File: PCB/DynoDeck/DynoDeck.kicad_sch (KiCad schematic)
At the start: 8 parts, among them J1 USB_C_Receptacle_USB2.0_16P, J2 E-paper, J3 CardKB, U1 E73-2G4M08S1C, U2 SX1262IMLTRT, U3 BQ25895RTW, U4 AMS1117-3.3, U5 TPS613222ADBV

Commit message: Schematic Power Circuit
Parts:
- removed U5: TPS613222ADBV, Package_TO_SOT_SMD:SOT-23-5, symbol Regulator_Switching:TPS613222ADBV
- added BT1: Batt, symbol Device:Battery
- added C1: 100n, symbol Device:C_Small
- added C10, C11, C6, C7, C8: 10u, symbol Device:C_Small
- added C12, C4: 4u7, symbol Device:C_Small
- added C2: 1u, symbol Device:C_Small
- added C3: 220n, symbol Device:C_Small
- added C5: 47n, symbol Device:C_Small
- added C9: 47u, symbol Device:C_Small
- added D1: STAT, symbol Device:LED_Small
- added D2: D_Schottky, symbol Device:D_Schottky_Small
- added L1: 2u2, symbol Device:L
- added R1, R2: 5k1, symbol Device:R_Small
- added R10, R6, R7, R9: 10k, symbol Device:R_Small
- added R11: 2k2, symbol Device:R_Small
- added R3, R4, R5: 4k7, symbol Device:R_Small
- added R8: 260, symbol Device:R_Small
- added SW1: QON, symbol Switch:SW_Push
- added U6: USBLC6-2SC6, Package_TO_SOT_SMD:SOT-23-6, symbol Power_Protection:USBLC6-2SC6
- J1: footprint (none) -> Connector_USB:USB_C_Receptacle_G-Switch_GT-USB-7010ASV
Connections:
- net +5V is gone; now on net +3V3: J3.3 (Pin_3)
- net +3V3: now also U4.2 (VO), C11.1, R3.1, R4.1, R5.1
- net GND: now also J1.A1 (GND), J1.A12 (GND), J1.B1 (GND), J1.B12 (GND), J1.SH (SHIELD), U3.17 (PGND), U3.18 (PGND), U3.25 (PGND), U4.1 (GND), BT1.2 (-), C1.2, C10.2, C11.2, C12.2, C2.2, C3.2, C4.2, C6.2, C7.2, C8.2, C9.2, R1.2, R10.2, R2.2, R6.2, R7.2, R8.2, SW1.2, U6.2 (GND)
- net SCL: now also U3.5 (SCL), R3.2; no longer J2.5 (Pin_5)
- net SDA: now also U3.6 (SDA), R4.2; no longer J2.6 (Pin_6)
- net VBUS: now reaches J1.A4 (VBUS), J1.A9 (VBUS), J1.B4 (VBUS), J1.B9 (VBUS)
- net VBUS: now also U1.27 (VBUS), U3.1 (VBUS), C1.1, C12.1, C2.1, C3.1, C9.1, D2.1 (K), U6.5 (VBUS)
- net at J1.A5 (CC1): now also R1.1
- net DIn+: now reaches J1.A6 (D+)
- net DIn+: now also J1.B6 (D+), U6.3 (I/O2)
- net DIn-: now reaches J1.A7 (D-)
- net DIn-: now also J1.B7 (D-), U6.1 (I/O1)
- net at J1.B5 (CC2): now also R2.1
- net D-: now reaches U1.29 (DM)
- net D-: now also U3.3 (D-), U6.6 (I/O1)
- net D+: now reaches U1.31 (DP)
- net D+: now also U3.2 (D+), U6.4 (I/O2)
- net SYS: now reaches U4.3 (VI)
- net SYS: now also U3.15 (SYS), U3.16 (SYS), C10.1, C7.1, C8.1, D1.2 (A), L1.2
- net at U3.10 (ILIM): now also R8.1
- net at U3.11 (TS): now also R10.1, R9.2
- net at U3.12 (~{QON}): now also SW1.1
- net BATT+: now reaches U3.13 (BAT), U3.14 (BAT)
- net BATT+: now also BT1.1 (+), C6.1
- net at U3.19 (SW), U3.20 (SW): now also C5.1, L1.1
- net at U3.21 (BTST): now also C5.2
- net at U3.22 (REGN): now also C4.1, R9.1
- net at U3.23 (PMID): now also D2.2 (A)
- net at U3.4 (STAT): now also R11.2
- net ~{INT}: now reaches U3.7 (~{INT})
- net ~{INT}: now also R5.2
- net OTG: now reaches U3.8 (OTG)
- net OTG: now also R6.1
- net ~{CE}: now reaches U3.9 (~{CE})
- net ~{CE}: now also R7.1
- new net: D1.1 (K), R11.1
- new net CLK: J2.5 (Pin_5)
- new net MOSI: J2.6 (Pin_6)
- no-connect marks 0 -> 3
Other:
- note added: "USBC + ESD"
- moved on the sheet: J1, J2, J3, U1A, U1C, U2, U3, U4

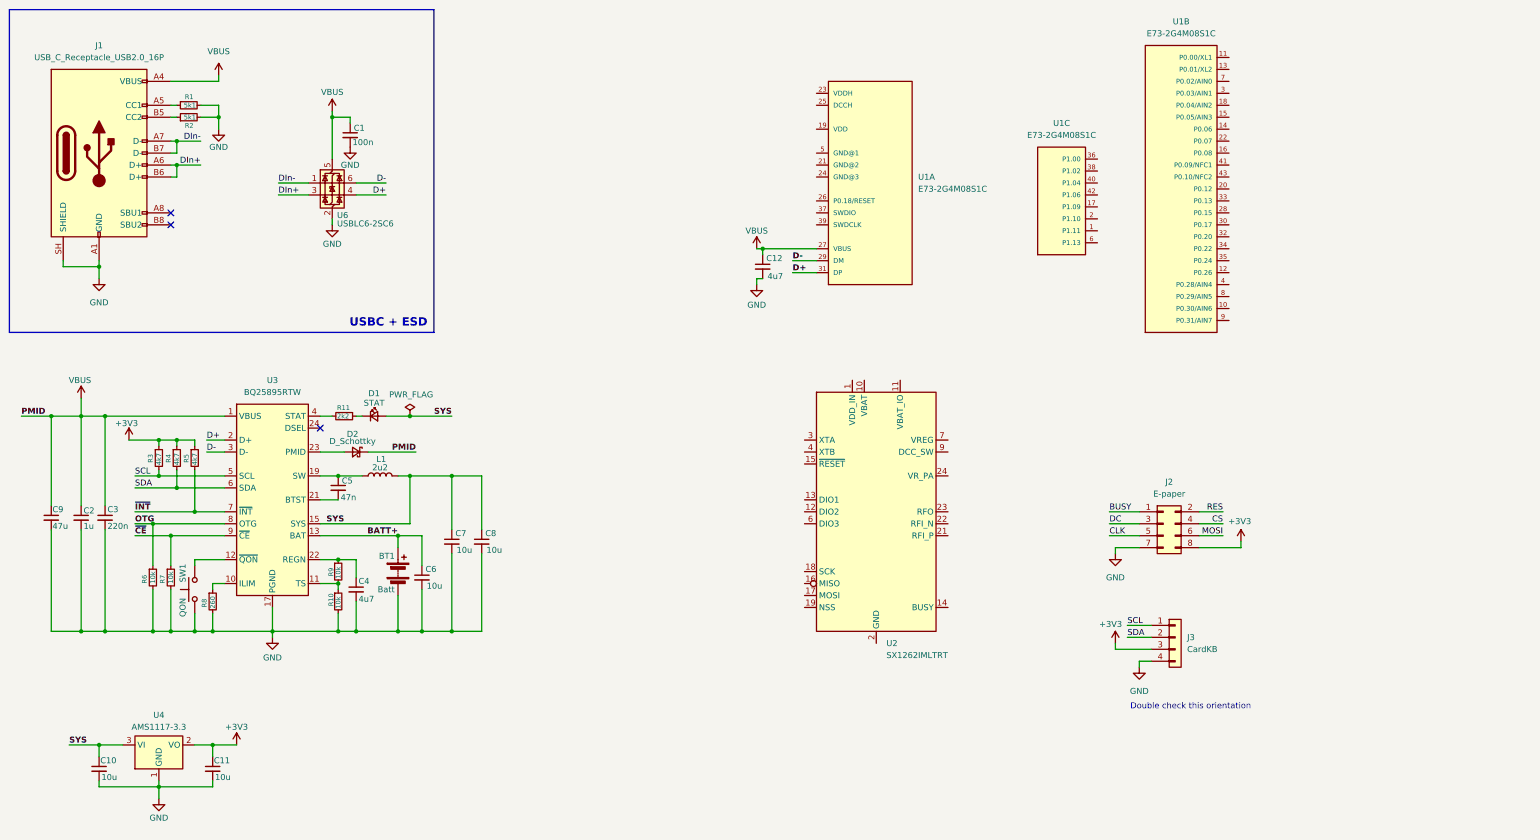
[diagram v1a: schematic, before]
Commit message: Power for nRf + SX1262
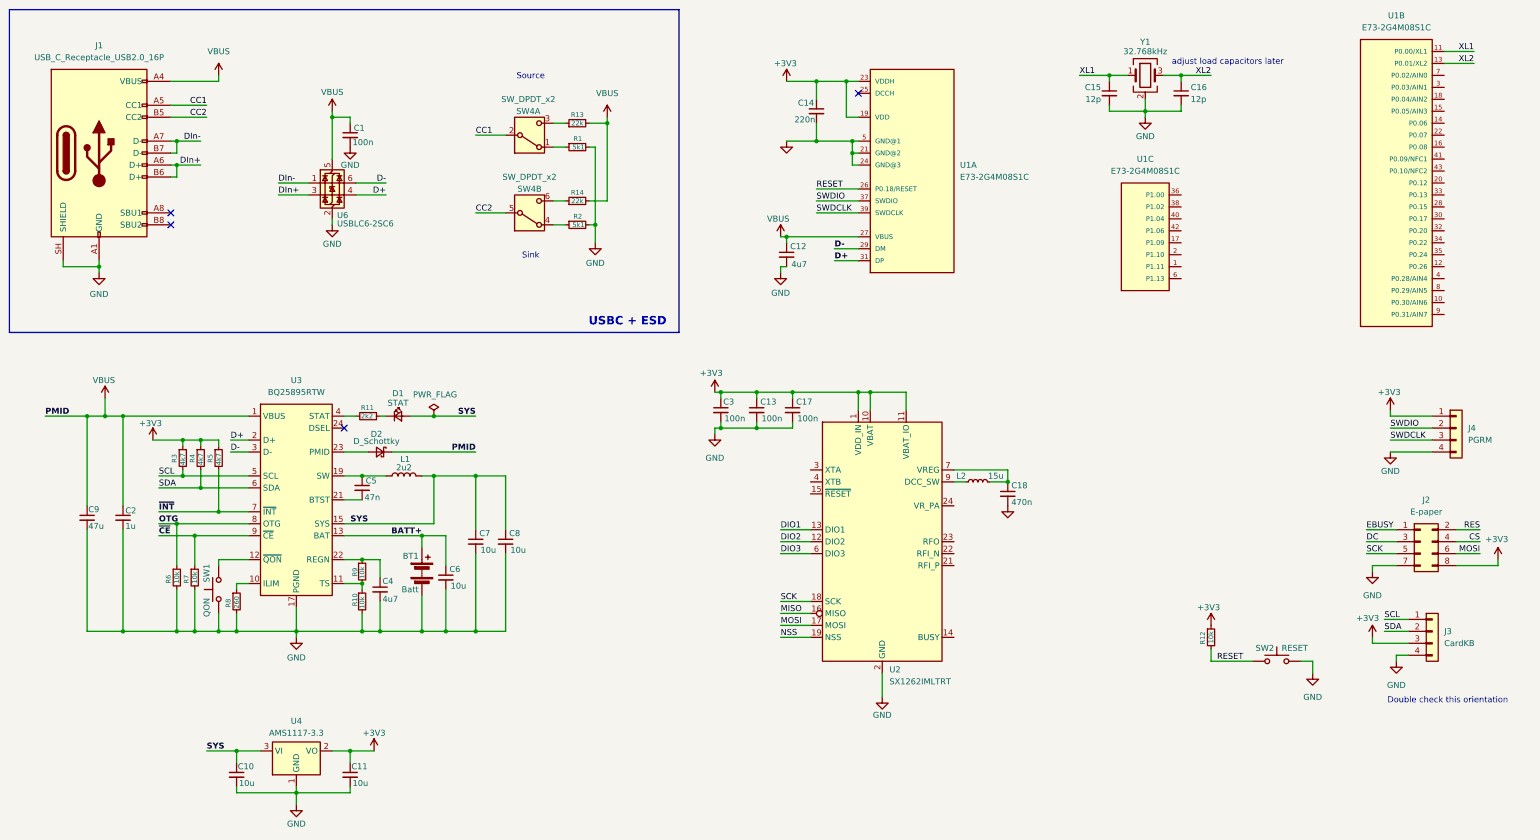
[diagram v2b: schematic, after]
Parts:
- added C13, C17: 100n, symbol Device:C_Small
- added C14: 220n, symbol Device:C_Small
- added C15, C16: 12p, symbol Device:C_Small
- added C18: 470n, symbol Device:C_Small
- added J4: PGRM, symbol Connector_Generic:Conn_01x04
- added L2: 15u, symbol Device:L_Small
- added R12: 10k, symbol Device:R_Small
- added R13, R14: 22k, symbol Device:R_Small
- added SW2: RESET, symbol Switch:SW_Push
- added SW4: SW_DPDT_x2, symbol Switch:SW_DPDT_x2
- added Y1: 32.768kHz, symbol Device:Crystal_GND24
- C3: value 220n -> 100n
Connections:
- net CLK is gone; now on net SCK: J2.5 (Pin_5)
- net +3V3: now also C3.1, U1.19 (VDD), U1.23 (VDDH), U2.1 (VDD_IN), U2.10 (VBAT), U2.11 (VBAT_IO), C13.1, C14.1, C17.1, J4.1 (Pin_1), R12.1
- net GND: now also U1.21 (GND@2), U1.24 (GND@3), U1.5 (GND@1), U2.2 (GND), U2.20 (GND), U2.25 (GND), U2.5 (GND), U2.8 (GND), C13.2, C14.2, C15.2, C16.2, C17.2, C18.2, J4.4 (Pin_4), SW2.2, Y1.2 (G), Y1.4 (G)
- net MOSI: now also U2.17 (MOSI)
- net VBUS: now also R13.2, R14.2; no longer C3.1
- net at R1.1: now also SW4.1 (A); no longer J1.A5 (CC1)
- net at R2.1: now also SW4.4 (A); no longer J1.B5 (CC2)
- net RESET: now reaches U1.26 (P0.18/RESET)
- net RESET: now also R12.2, SW2.1
- net SWDIO: now reaches U1.37 (SWDIO)
- net SWDIO: now also J4.2 (Pin_2)
- net SWDCLK: now reaches U1.39 (SWDCLK)
- net SWDCLK: now also J4.3 (Pin_3)
- net XL1: now reaches U1.11 (P0.00/XL1)
- net XL1: now also C15.1, Y1.1
- net XL2: now reaches U1.13 (P0.01/XL2)
- net XL2: now also C16.1, Y1.3
- net DIO2: now reaches U2.12 (DIO2)
- net DIO1: now reaches U2.13 (DIO1)
- net MISO: now reaches U2.16 (MISO)
- net SCK: now reaches U2.18 (SCK)
- net NSS: now reaches U2.19 (NSS)
- net DIO3: now reaches U2.6 (DIO3)
- net at U2.7 (VREG): now also C18.1, L2.1
- net at U2.9 (DCC_SW): now also L2.2
- net BUSY renamed EBUSY
- new net: R13.1, SW4.3 (C)
- new net: R14.1, SW4.6 (C)
- new net CC1: J1.A5 (CC1), SW4.2 (B)
- new net CC2: J1.B5 (CC2), SW4.5 (B)
- no-connect marks 3 -> 4
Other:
- note added: "Sink"
- note added: "Source"
- note added: "adjust load capacitors later"
- moved on the sheet: BT1, C10, C11, C12, C2, C4, C5, C6, C7, C8, C9, D1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

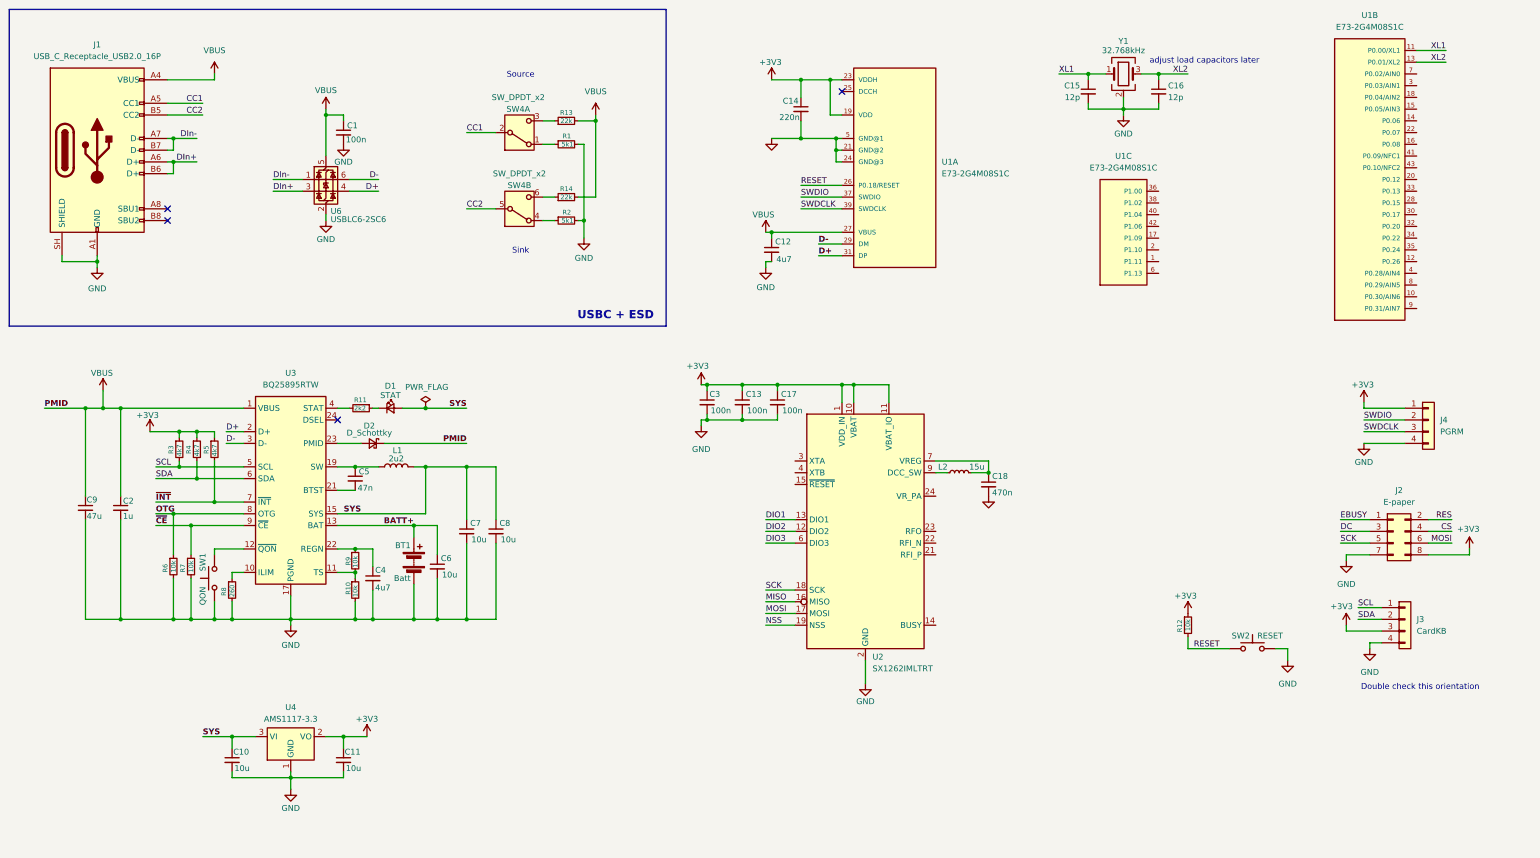
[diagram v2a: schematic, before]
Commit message: Part of SX1262 Power + Signals
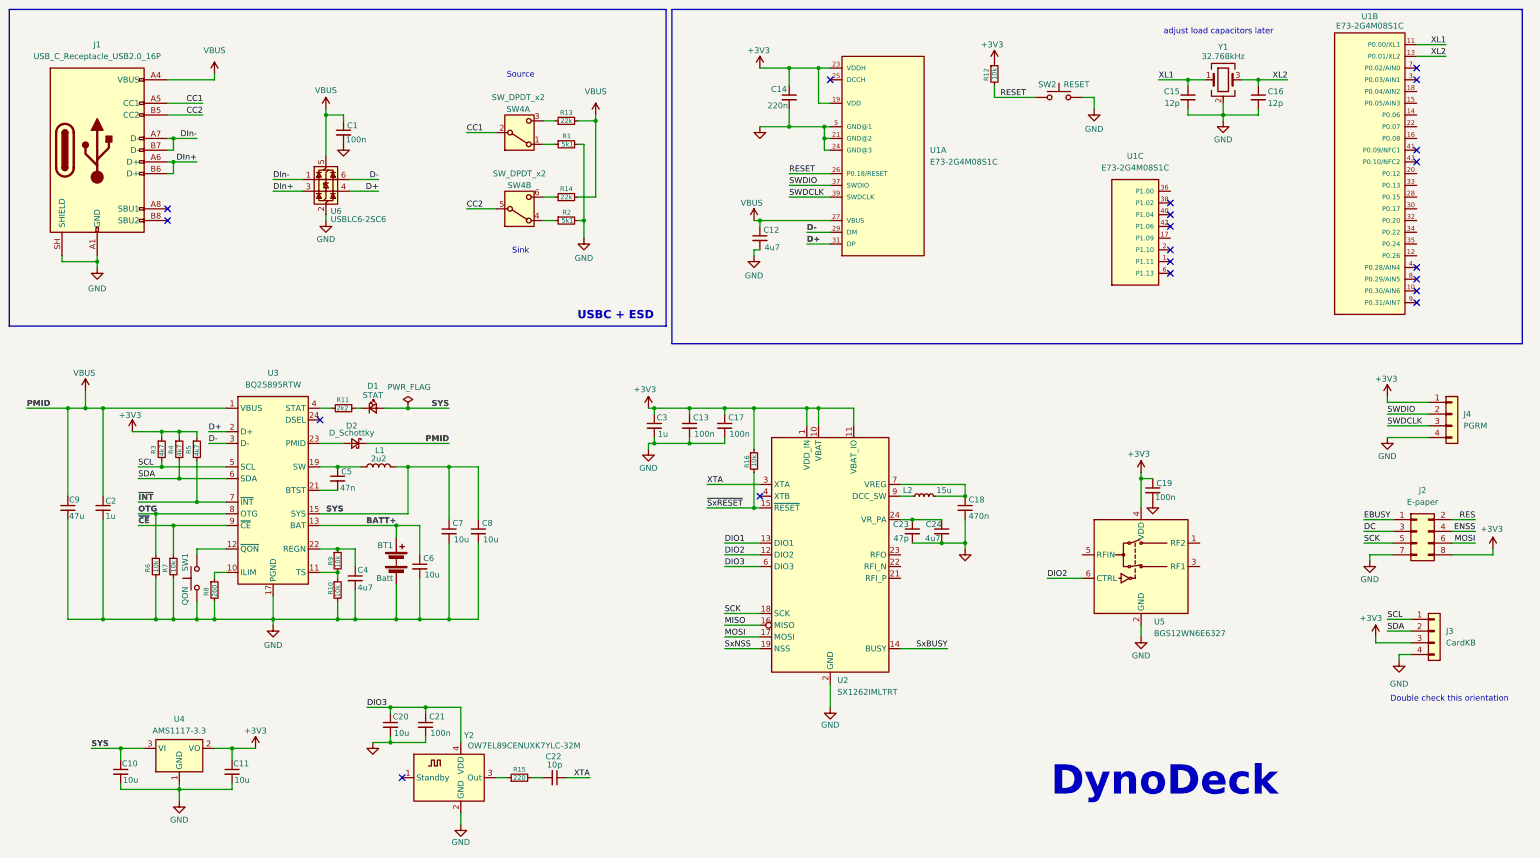
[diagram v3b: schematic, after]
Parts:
- added C19, C21: 100n, symbol Device:C_Small
- added C20: 10u, symbol Device:C_Small
- added C22: 10p, symbol Device:C_Small
- added C23: 47p, symbol Device:C_Small
- added C24: 4u7, symbol Device:C_Small
- added R15: 220, symbol Device:R_Small
- added R16: 10k, symbol Device:R_Small
- added U5: BGS12WN6E6327, Package_LGA:Infineon_PG-TSNP-6-10_0.7x1.1mm_0.7x1.1mm_P0.4mm, symbol RF_Switch:BGS12WN6E6327
- added Y2: OW7EL89CENUXK7YLC-32M, Oscillator:Oscillator_SMD_Abracon_ASDMB-4Pin_2.5x2.0mm, symbol Oscillator:ASDMB-xxxMHz
- C3: value 100n -> 1u
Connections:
- net +3V3: now also C19.1, R16.1, U5.4 (VDD)
- net DIO2: now also U5.6 (CTRL)
- net DIO3: now also C20.1, C21.1, Y2.4 (VDD)
- net GND: now also C19.2, C20.2, C21.2, C23.2, C24.2, U5.2 (GND), Y2.2 (GND)
- net SxBUSY: now reaches U2.14 (BUSY)
- net ~{SxRESET}: now reaches U2.15 (~{RESET})
- net ~{SxRESET}: now also R16.2
- net at U2.24 (VR_PA): now also C23.1, C24.1
- net XTA: now reaches U2.3 (XTA)
- net XTA: now also C22.1
- net CS renamed ENSS
- net NSS renamed SxNSS
- new net: C22.2, R15.2
- new net: R15.1, Y2.3 (Out)
- no-connect marks 4 -> 20
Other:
- note added: "DynoDeck"
- moved on the sheet: BT1, C10, C11, C12, C13, C14, C15, C16, C17, C18, C2, C3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
